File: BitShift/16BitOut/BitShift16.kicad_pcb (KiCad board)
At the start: 2 copper layers, 53.3 x 53.3 mm, 9 parts, among them U1 74AHC595, U2 74AHC595

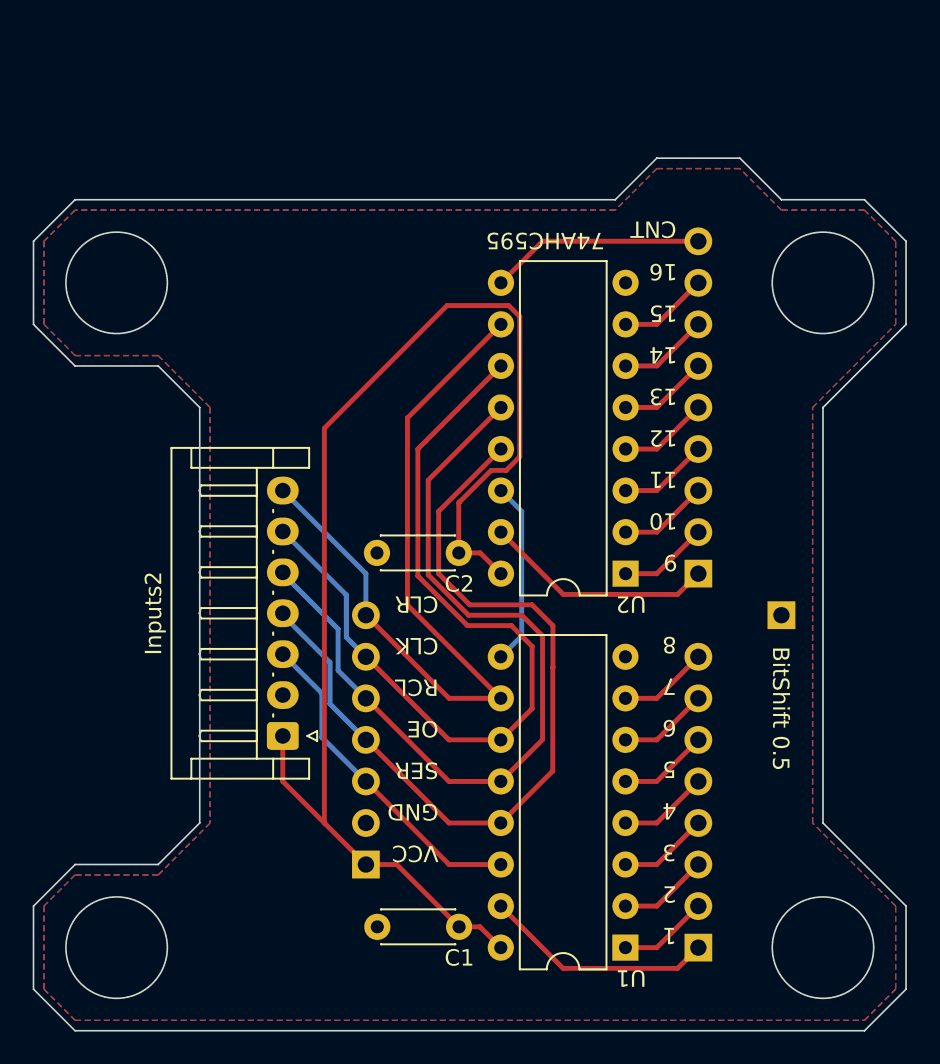
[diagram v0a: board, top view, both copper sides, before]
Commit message: updated bitshift, dual7 and dualbitshift
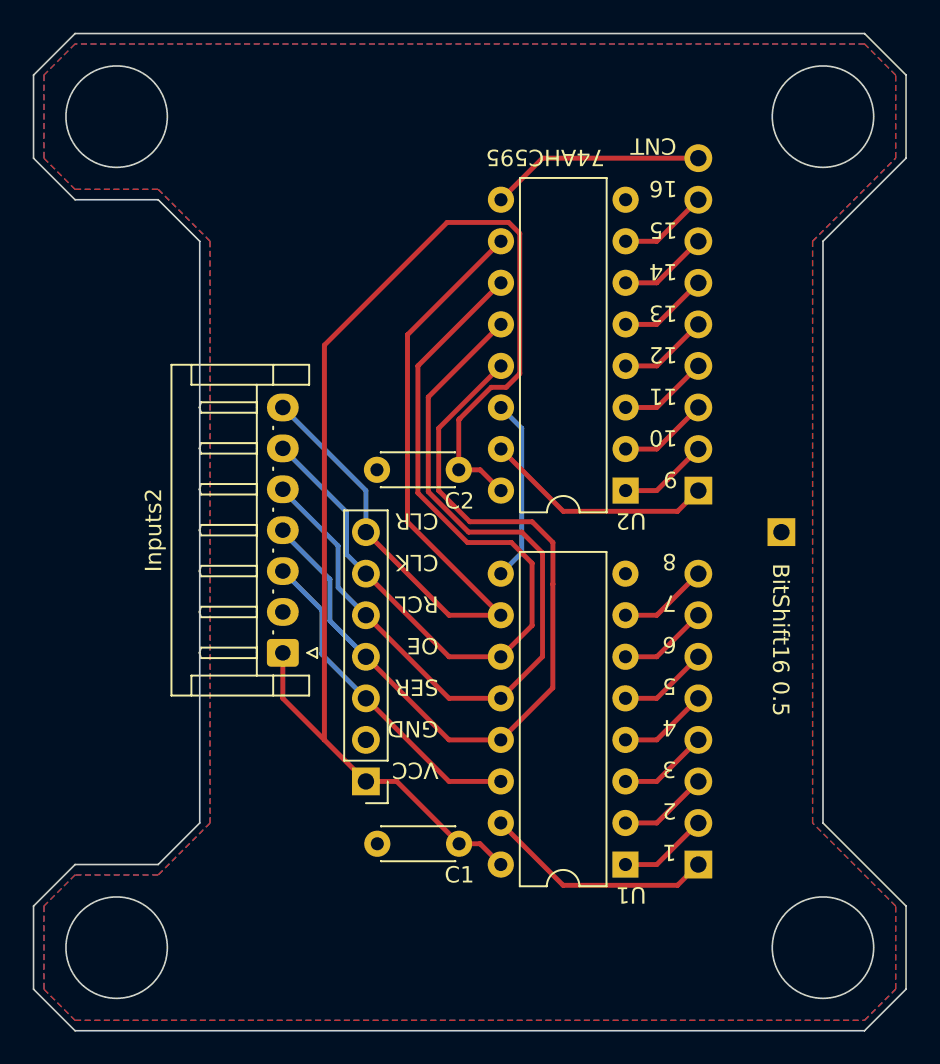
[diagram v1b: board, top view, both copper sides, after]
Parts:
- Inputs1: moved to F.Cu
- moved C2 5.08 mm to (97.1, 62.2)
- moved C1 5.08 mm to (97.1, 85.1)
- moved GND2 5.08 mm to (116.8, 66.0)
- moved Inputs1 5.08 mm to (91.4, 81.3), turned to 180 degrees
- moved Inputs2 5.08 mm to (86.4, 73.4)
- moved Outputs1 5.08 mm to (111.8, 86.4)
- moved Outputs2 5.08 mm to (111.8, 63.5)
- moved U1 5.08 mm to (107.3, 86.4)
- moved U2 5.08 mm to (107.3, 63.5)
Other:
- board size 53.3 x 53.3 mm -> 53.3 x 61 mm
- board text added: "BitShift16 0.5"
- board text removed: "BitShift 0.5"
